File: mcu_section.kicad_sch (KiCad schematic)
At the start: 21 parts, among them SW1 Reset, SW2 Boot, U1 ESP32-D0WDQ6, Y1 ABM10AIG

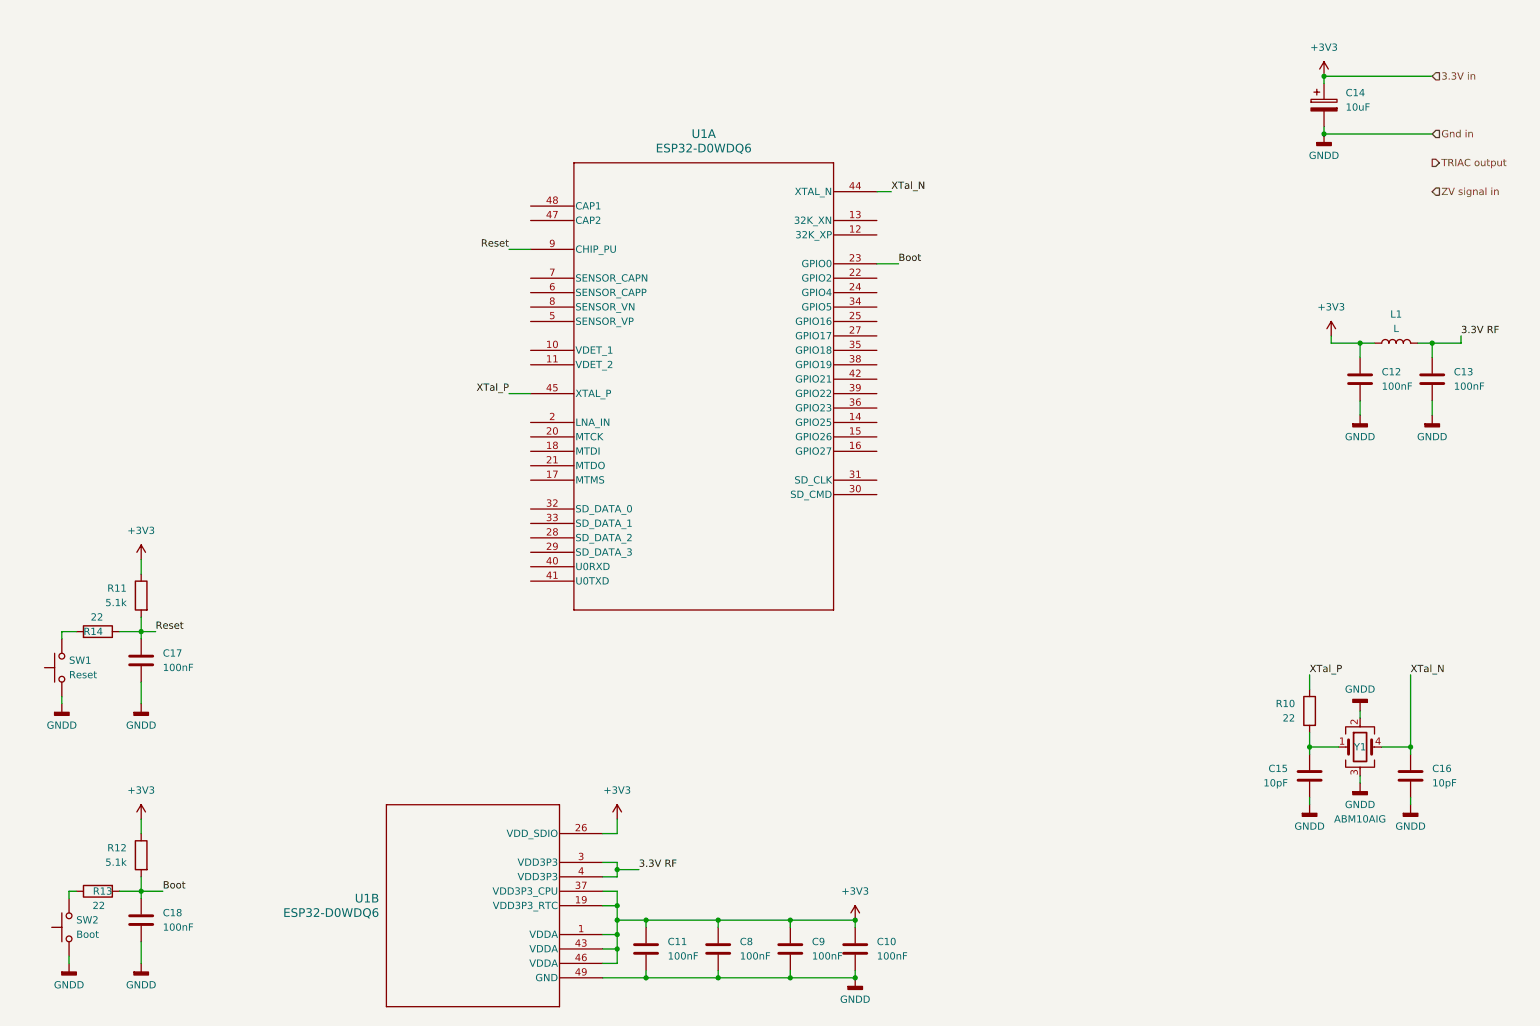
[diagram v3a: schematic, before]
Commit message: added flash, uart
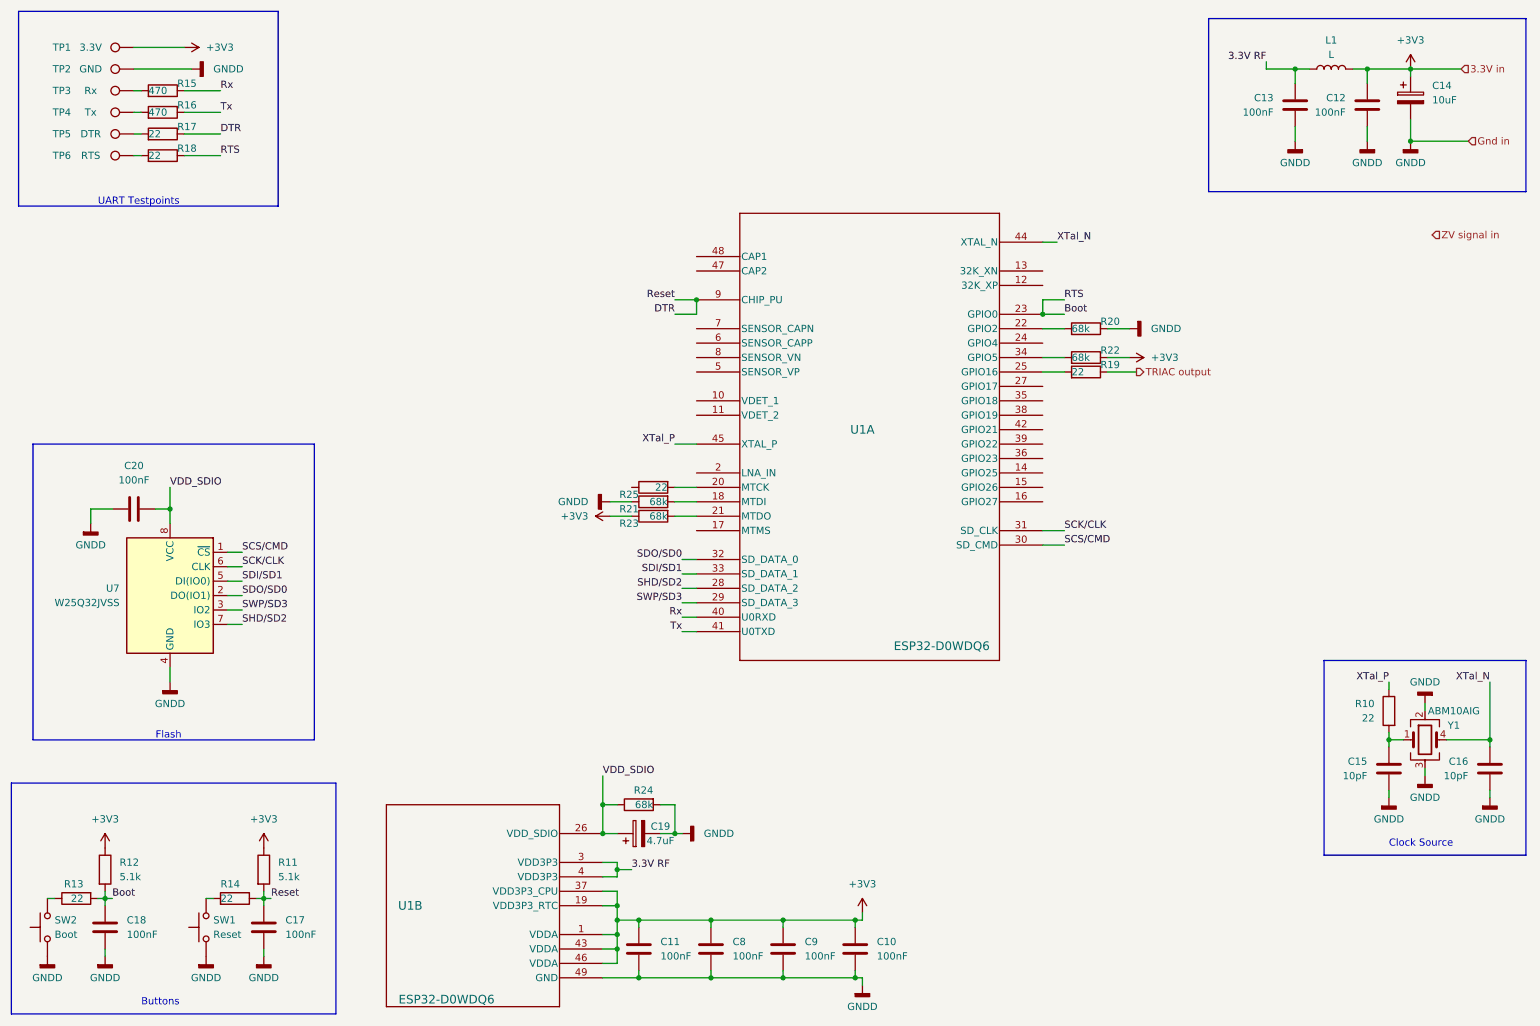
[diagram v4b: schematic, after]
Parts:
- added C19: 4.7uF, Capacitor_Tantalum_SMD:CP_EIA-6032-20_AVX-F_Pad2.25x2.35mm_HandSolder, symbol Device:C_Polarized
- added C20: 100nF, Capacitor_SMD:C_1206_3216Metric, symbol Device:C
- added R15, R16: 470, Resistor_SMD:R_0603_1608Metric_Pad0.98x0.95mm_HandSolder, symbol Device:R
- added R17, R18, R19, R25: 22, Resistor_SMD:R_0603_1608Metric_Pad0.98x0.95mm_HandSolder, symbol Device:R
- added R20, R21, R22, R23, R24: 68k, Resistor_SMD:R_0603_1608Metric_Pad0.98x0.95mm_HandSolder, symbol Device:R
- added TP1: 3.3V, TestPoint:TestPoint_Pad_D1.5mm, symbol Connector:TestPoint
- added TP2: GND, TestPoint:TestPoint_Pad_D1.5mm, symbol Connector:TestPoint
- added TP3: Rx, TestPoint:TestPoint_Pad_D1.5mm, symbol Connector:TestPoint
- added TP4: Tx, TestPoint:TestPoint_Pad_D1.5mm, symbol Connector:TestPoint
- added TP5: DTR, TestPoint:TestPoint_Pad_D1.5mm, symbol Connector:TestPoint
- added TP6: RTS, TestPoint:TestPoint_Pad_D1.5mm, symbol Connector:TestPoint
- added U7: W25Q32JVSS, Package_SO:SOIC-8_5.23x5.23mm_P1.27mm, symbol Memory_Flash:W25Q32JVSS
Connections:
- net +3V3: now also R22.1, R23.1, TP1.1; no longer U1.26 (VDD_SDIO)
- net Boot: now also R18.1
- net GNDD: now also C19.2, C20.2, R20.1, R21.1, R24.2, TP2.1, U7.4 (GND)
- net TRIAC output: now also R19.1
- net at U1.18 (MTDI): now also R21.2
- net at U1.20 (MTCK): now also R25.2
- net at U1.21 (MTDO): now also R23.2
- net at U1.22 (GPIO2): now also R20.2
- net at U1.25 (GPIO16): now also R19.2
- net SHD/SD2: now reaches U1.28 (SD_DATA_2)
- net SHD/SD2: now also U7.7 (IO3)
- net SWP/SD3: now reaches U1.29 (SD_DATA_3)
- net SWP/SD3: now also U7.3 (IO2)
- net SCS/CMD: now reaches U1.30 (SD_CMD)
- net SCS/CMD: now also U7.1 (~{CS})
- net SCK/CLK: now reaches U1.31 (SD_CLK)
- net SCK/CLK: now also U7.6 (CLK)
- net SDO/SD0: now reaches U1.32 (SD_DATA_0)
- net SDO/SD0: now also U7.2 (DO(IO1))
- net SDI/SD1: now reaches U1.33 (SD_DATA_1)
- net SDI/SD1: now also U7.5 (DI(IO0))
- net at U1.34 (GPIO5): now also R22.2
- net Rx: now reaches U1.40 (U0RXD)
- net Rx: now also R15.1
- net Tx: now reaches U1.41 (U0TXD)
- net Tx: now also R16.1
- net Reset renamed DTR
- net DTR: now also R17.1
- new net: R16.2, TP4.1
- new net: R18.2, TP6.1
- new net: R17.2, TP5.1
- new net: R15.2, TP3.1
- new net VDD_SDIO: C19.1, C20.1, R24.1, U1.26 (VDD_SDIO), U7.8 (VCC)
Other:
- note added: "Buttons"
- note added: "Clock Source"
- note added: "Flash"
- note added: "UART Testpoints"
- moved on the sheet: C11, C12, C13, C14, C15, C16, C17, C18, C8, C9, L1, R10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

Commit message: added antenna symbol
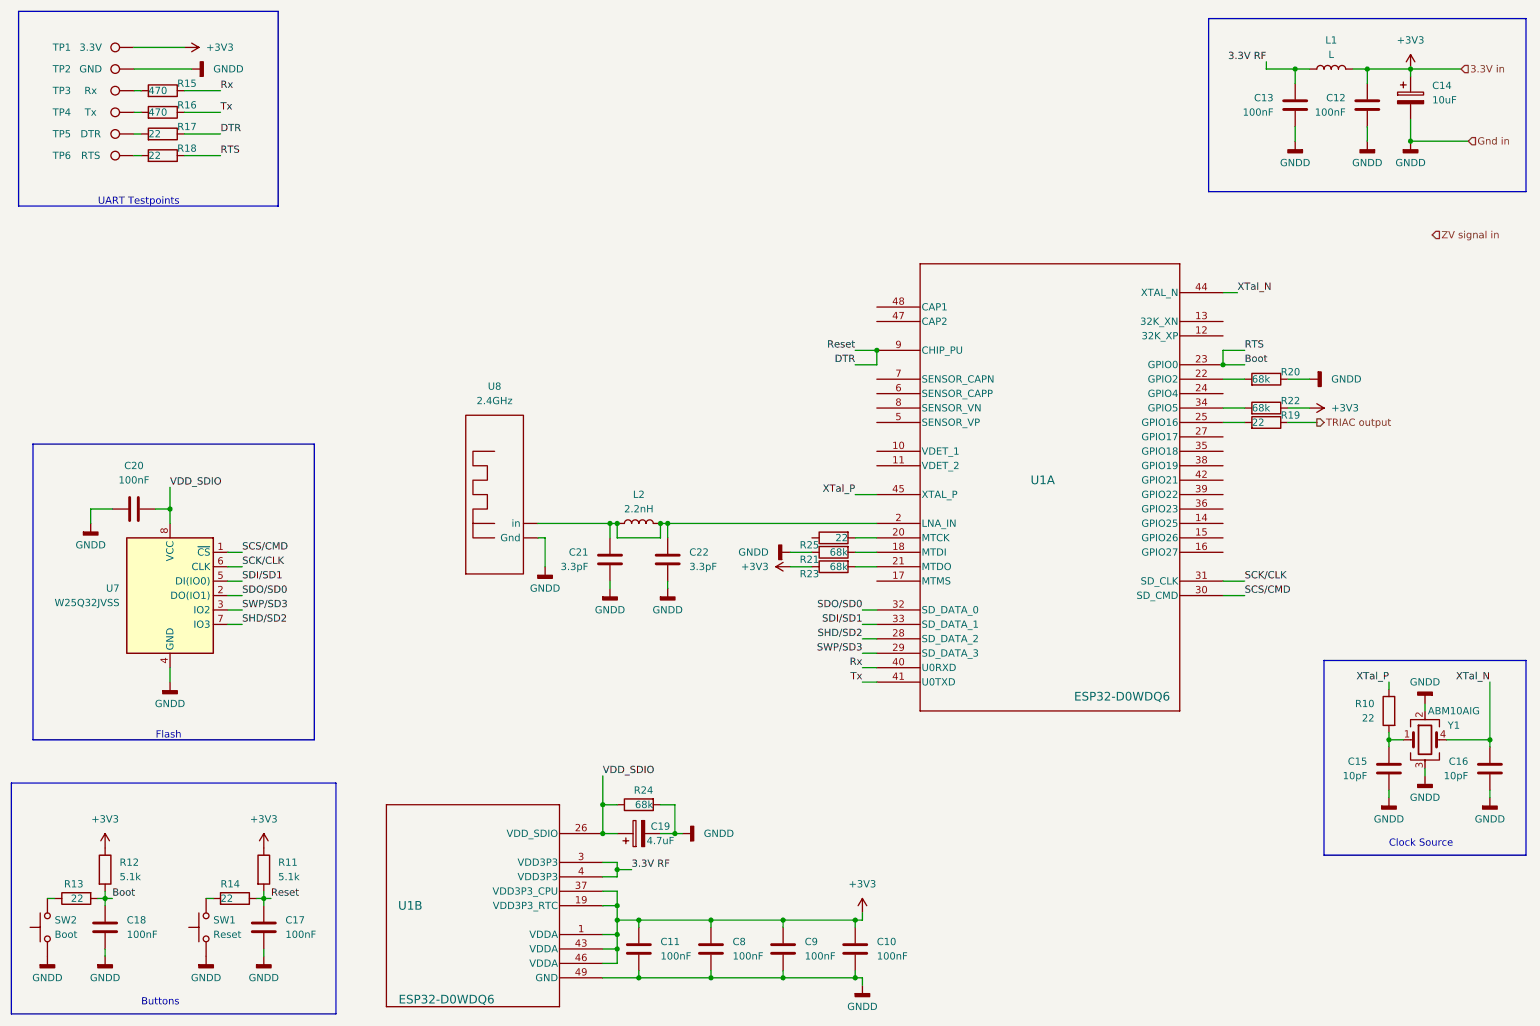
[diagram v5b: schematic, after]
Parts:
- added C21, C22: 3.3pF, Capacitor_SMD:C_0402_1005Metric, symbol Device:C
- added L2: 2.2nH, Inductor_SMD:L_0402_1005Metric_Pad0.77x0.64mm_HandSolder, symbol Device:L
- added U8: 2.4GHz, symbol pcb_ant_2G4Hz:ANT_2.4GHz
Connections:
- net GNDD: now also C21.2, C22.2, U8. (in)
- net at U1.2 (LNA_IN): now also C21.1, C22.1, L2.1, L2.2, U8. (in)
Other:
- moved on the sheet: R19, R20, R21, R22, R23, R25, U1A

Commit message: schematic completed:
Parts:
- removed U8: 2.4GHz, symbol pcb_ant_2G4Hz:ANT_2.4GHz
- added U8: ANTENNA 2.4GHz, RF_Antenna:Texas_SWRA117D_2.4GHz_Right, symbol pcb antenna 2G4Hz:ANTENNA 2.4GHz
- L1: value L -> 2.2nH; footprint (none) -> Inductor_SMD:L_1210_3225Metric_Pad1.42x2.65mm_HandSolder
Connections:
- net GNDD: now also U8.2 (Gnd)
- net at C21.1, C22.1, L2.1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: now also U8.1 (in)
- net ZVC signal in: now reaches U1.16 (GPIO27)
- no-connect marks 0 -> 20
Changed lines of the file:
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@@
   (junction (at 118.11 160.02) (diameter 0) (color 0 0 0 0)
   )
+  (no_connect (at 227.33 95.25))
+  (no_connect (at 227.33 102.87))
+  (no_connect (at 166.37 87.63))
+  (no_connect (at 227.33 82.55))
+  (no_connect (at 166.37 69.85))
+  (no_connect (at 227.33 72.39))
+  (no_connect (at 227.33 97.79))
+  (no_connect (at 166.37 80.01))
+  (no_connect (at 227.33 105.41))
+  (no_connect (at 166.37 92.71))
+  (no_connect (at 227.33 92.71))
+  (no_connect (at 166.37 85.09))
+  (no_connect (at 227.33 90.17))
+  (no_connect (at 166.37 95.25))
+  (no_connect (at 227.33 69.85))
+  (no_connect (at 227.33 107.95))
+  (no_connect (at 166.37 115.57))
+  (no_connect (at 227.33 100.33))
+  (no_connect (at 166.37 67.31))
+  (no_connect (at 166.37 82.55))
   (wire (pts (xy 30.48 171.45) (xy 31.75 171.45))
     (stroke (width 0) (type default))
@@
   )
   (wire (pts (xy 137.16 184.15) (xy 137.16 185.42))
+    (stroke (width 0) (type default))
+  )
+  (wire (pts (xy 227.33 110.49) (xy 231.14 110.49))
     (stroke (width 0) (type default))
   )
@@
     (effects (font (size 1.27 1.27)) (justify left))
   )
-  (hierarchical_label "ZV signal in" (shape input) (at 264.16 54.61 0) (fields_autoplaced)
+  (hierarchical_label "ZVC signal in" (shape input) (at 231.14 110.49 0) (fields_autoplaced)
     (effects (font (size 1.27 1.27)) (justify left))
   )
@@
         (path "/45e1e5e5-a388-432c-8d2b-80b7f8345075/1dc68658-e7d3-43ab-9cff-123756104291"
           (reference "#PWR04") (unit 1)
+        )
+      )
+    )
+  )
+  (symbol (lib_id "pcb antenna 2G4Hz:ANTENNA 2.4GHz") (at 99.06 100.33 90) (unit 1)
+    (in_bom yes) (on_board yes) (dnp no) (fields_autoplaced)
+    (property "Reference" "U8" (at 99.06 81.28 90)
+      (effects (font (size 1.27 1.27)))
+    )
+    (property "Value" "ANTENNA 2.4GHz" (at 99.06 83.82 90)
+      (effects (font (size 1.27 1.27)))
+    )
+    (property "Footprint" "RF_Antenna:Texas_SWRA117D_2.4GHz_Right" (at 99.06 100.33 0)
+      (effects (font (size 1.27 1.27)) hide)
+    )
+    (property "Datasheet" "" (at 99.06 100.33 0)
+      (effects (font (size 1.27 1.27)) hide)
+    )
+    (pin "1")
+    (pin "2")
+    (instances
+      (project "esp32-iot-socket"
+        (path "/45e1e5e5-a388-432c-8d2b-80b7f8345075/1dc68658-e7d3-43ab-9cff-123756104291"
+          (reference "U8") (unit 1)
         )
       )
@@
     )
   )
-  (symbol (lib_id "pcb_ant_2G4Hz:ANT_2.4GHz") (at 99.06 100.33 90) (unit 1)
-    (in_bom yes) (on_board yes) (dnp no) (fields_autoplaced)
-    (property "Reference" "U8" (at 99.06 81.28 90)
-      (effects (font (size 1.27 1.27)))
-    )
-    (property "Value" "2.4GHz" (at 99.06 83.82 90)
-      (effects (font (size 1.27 1.27)))
-    )
-    (property "Footprint" "" (at 99.06 100.33 0)
-      (effects (font (size 1.27 1.27)) hide)
-    )
-    (property "Datasheet" "" (at 99.06 100.33 0)
-      (effects (font (size 1.27 1.27)) hide)
-    )
-    (pin "")
-    (pin "")
-    (instances
-      (project "esp32-iot-socket"
-        (path "/45e1e5e5-a388-432c-8d2b-80b7f8345075/1dc68658-e7d3-43ab-9cff-123756104291"
-          (reference "U8") (unit 1)
-        )
-      )
-    )
-  )
   (symbol (lib_id "power:GNDD") (at 45.72 25.4 90) (unit 1)
     (in_bom yes) (on_board yes) (dnp no) (fields_autoplaced)
@@
       (effects (font (size 1.27 1.27)))
     )
-    (property "Value" "L" (at 246.38 22.86 90)
-      (effects (font (size 1.27 1.27)))
-    )
-    (property "Footprint" "" (at 246.38 25.4 0)
-      (effects (font (size 1.27 1.27)) hide)
-    )
+    (property "Value" "2.2nH" (at 246.38 22.86 90)
+      (effects (font (size 1.27 1.27)))
+    )
+    (property "Footprint" "Inductor_SMD:L_1210_3225Metric_Pad1.42x2.65mm_HandSolder" (at 246.38 25.4 0)
+      (effects (font (size 1.27 1.27)) hide)
+    )
